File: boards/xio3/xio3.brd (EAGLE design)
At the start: 170 x 170 mm, 148 parts

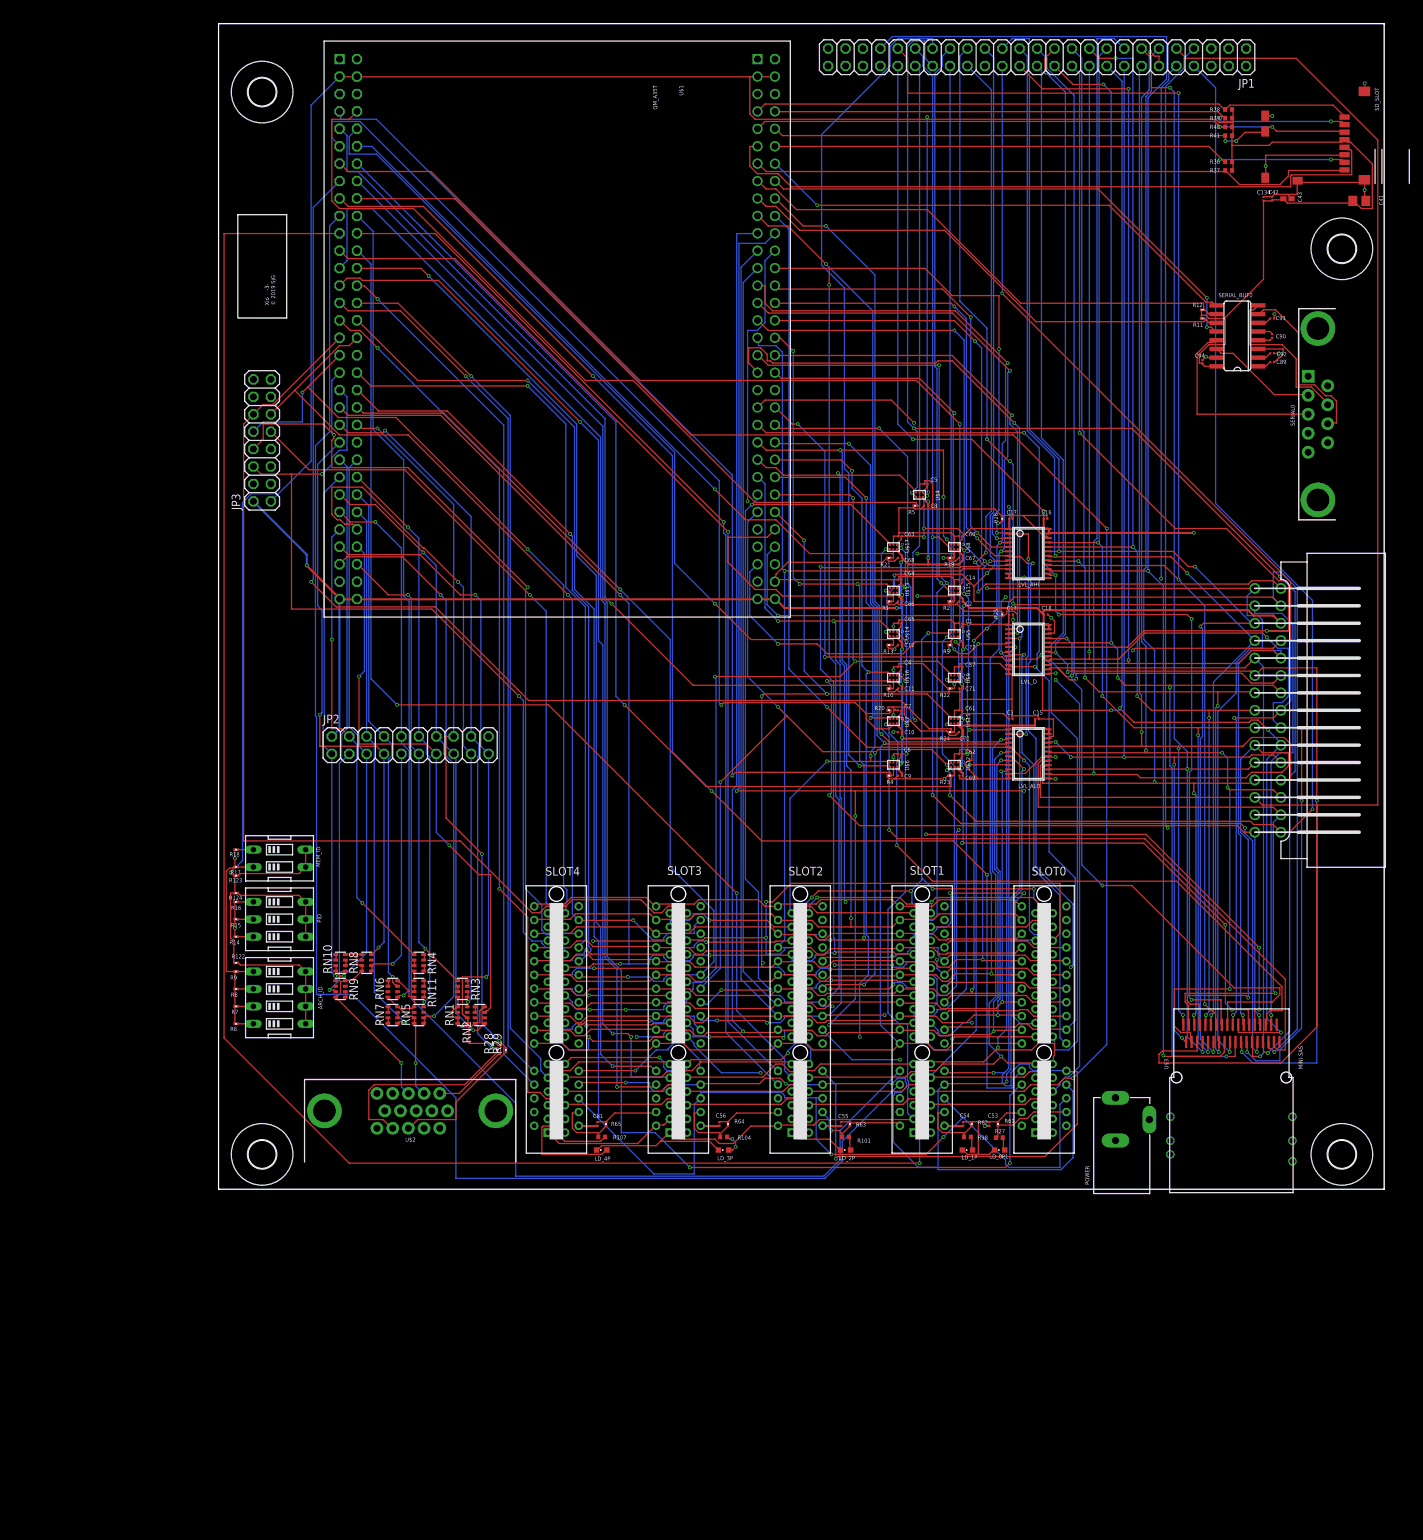
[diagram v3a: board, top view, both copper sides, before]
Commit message: - Add a +5v plane to cover where useful - Have a better placement of the HBUS extension - Gives at least 10cm of space for cards
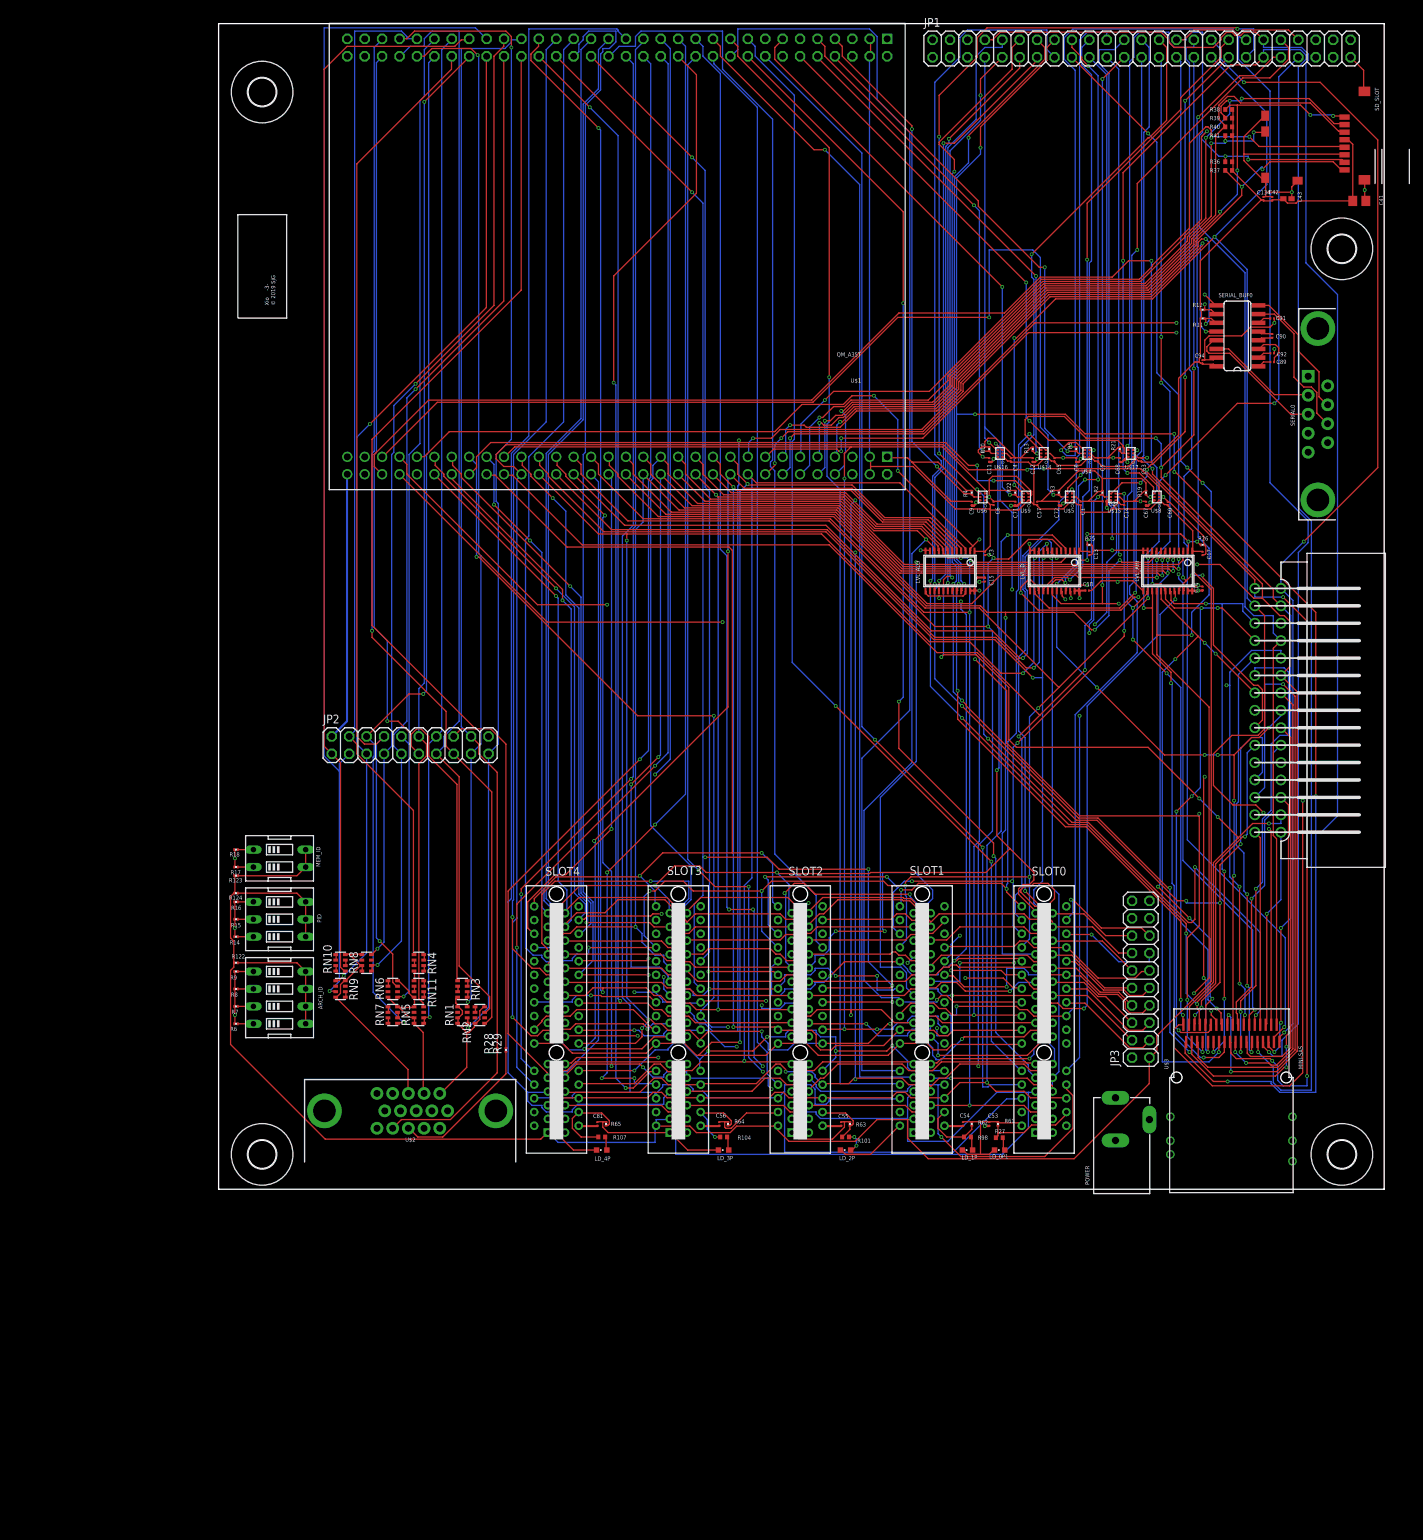
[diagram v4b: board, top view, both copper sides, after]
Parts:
- removed C10, C61, C62, C64, C66, C69, C7, C70: 0.1uF, rcl:C0201
- removed R1, R20, R23, R24: 10K, rcl:R0201
- removed U$11, U$12, U$13, U$7: 74LVC1T45GWSOT866, sjg-logic:SOT886
- JP3: device pinhead:2X08 -> pinhead:2X10
- moved JP3 150.3 mm to (134.5, 30.6)
- moved R4 43.0 mm to (109.9, 101.6), turned to 90 degrees
- moved U$6 41.2 mm to (111.4, 101.0), turned to 180 degrees
- moved C9 41.0 mm to (109.9, 100.0), turned to 90 degrees
- moved C6 39.0 mm to (113.0, 100.0), turned to 90 degrees
- moved R10 37.9 mm to (112.4, 108.0), turned to 90 degrees
- moved R21 37.2 mm to (131.4, 108.0), turned to 90 degrees
- moved U$17 37.2 mm to (133.0, 107.3), turned to 180 degrees
- moved C63 37.0 mm to (134.6, 106.4), turned to 90 degrees
- moved U$16 36.2 mm to (114.0, 107.3), turned to 180 degrees
- moved C11 35.8 mm to (112.4, 106.4), turned to 90 degrees
- moved R13 35.4 mm to (118.7, 108.0), turned to 90 degrees
- moved C68 35.1 mm to (131.4, 106.4), turned to 90 degrees
- moved U$14 34.3 mm to (120.3, 107.3), turned to 180 degrees
- moved C4 34.2 mm to (115.6, 106.4), turned to 90 degrees
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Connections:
- removed net !HI_REF!: JP1.40, U$3.PB16, U$7.4
- removed net !LO_S4!: SLOT0.B20, SLOT1.B20, SLOT2.B20, SLOT3.B20, SLOT4.B20, U$1.U7_53, U$12.3
- removed net !LO_S5!: SLOT0.B21, SLOT1.B21, SLOT2.B21, SLOT3.B21, SLOT4.B21, U$1.U7_54, U$11.3
- new net HBUS10: JP3.13, SLOT0.B28, SLOT1.B28, SLOT2.B28, SLOT3.B28, SLOT4.B28, U$1.U7_51
- new net HBUS11: JP3.14, SLOT0.B29, SLOT1.B29, SLOT2.B29, SLOT3.B29, SLOT4.B29, U$1.U7_52
- new net HBUS12: JP3.15, SLOT0.B30, SLOT1.B30, SLOT2.B30, SLOT3.B30, SLOT4.B30, U$1.U7_53
- new net HBUS13: JP3.16, SLOT0.B31, SLOT1.B31, SLOT2.B31, SLOT3.B31, SLOT4.B31, U$1.U7_54
- net !HI_CCTL!: no longer U$13.4
- net !HI_S4!: now also JP1.40, U$3.PB16; no longer U$12.4
- net !HI_S5!: now also JP1.44, U$3.PB18; no longer U$11.4
- net !LO_CCTL!: no longer U$1.U7_34, U$13.3
- net !LO_EXTSEL!: now also U$1.U7_43; no longer U$1.U7_44
- net !LO_HALT!: now also SLOT0.B13, SLOT1.B13, SLOT2.B13, SLOT3.B13, SLOT4.B13, U$1.U7_44; no longer SLOT0.A30, SLOT1.A30, SLOT2.A30, SLOT3.A30, SLOT4.A30, U$1.U7_45
- net !LO_IRQ!: now also SLOT0.B14, SLOT1.B14, SLOT2.B14, SLOT3.B14, SLOT4.B14, U$1.U7_45; no longer SLOT0.A31, SLOT1.A31, SLOT2.A31, SLOT3.A31, SLOT4.A31, U$1.U7_46
- net !LO_MPD!: now also SLOT0.A30, SLOT1.A30, SLOT2.A30, SLOT3.A30, SLOT4.A30, U$1.U7_46; no longer SLOT0.A32, SLOT1.A32, SLOT2.A32, SLOT3.A32, SLOT4.A32, U$1.U7_47
- net !LO_REF!: now also SLOT0.B15, SLOT1.B15, SLOT2.B15, SLOT3.B15, SLOT4.B15; no longer SLOT0.B17, SLOT1.B17, SLOT2.B17, SLOT3.B17, SLOT4.B17, U$1.U7_50, U$7.3
- net !LO_RST!: now also SLOT0.B16, SLOT1.B16, SLOT2.B16, SLOT3.B16, SLOT4.B16, U$1.U7_49; no longer SLOT0.B18, SLOT1.B18, SLOT2.B18, SLOT3.B18, SLOT4.B18, U$1.U7_51
- net +3V3: no longer C61.1, C62.1, C64.1, C7.1, U$11.1, U$12.1, U$13.1, U$7.1
- net +5V: no longer C10.1, C66.1, C69.1, C70.1, U$11.6, U$12.6, U$13.6, U$7.6
- net DIR_CCTL: no longer R1.1, U$13.5
- net DIR_REF: no longer R20.1, U$7.5
- net DIR_S4: no longer R23.1, U$12.5
- net DIR_S5: no longer R24.1, U$11.5
- net GND: now also JP3.17, JP3.18, JP3.19, JP3.20, SLOT0.B32, SLOT1.B32, SLOT2.B32, SLOT3.B32, SLOT4.B32; no longer C10.2, C61.2, C62.2, C64.2, C66.2, C69.2, C7.2, C70.2, JP1.44, JP3.13, JP3.14, JP3.15, JP3.16, R1.2, R20.2, R23.2, R24.2, SLOT0.A6, SLOT0.A7, SLOT1.A6, SLOT1.A7, SLOT2.A6, SLOT2.A7, SLOT3.A6, SLOT3.A7, SLOT4.A6, U$11.2, U$12.2, U$13.2, U$7.2
- net HBUS0: now also SLOT0.B18, SLOT1.B18, SLOT2.B18, SLOT3.B18, SLOT4.B18; no longer SLOT0.B22, SLOT1.B22, SLOT2.B22, SLOT3.B22, SLOT4.B22
- net HBUS1: now also SLOT0.B19, SLOT1.B19, SLOT2.B19, SLOT3.B19, SLOT4.B19; no longer SLOT0.B23, SLOT1.B23, SLOT2.B23, SLOT3.B23, SLOT4.B23
- net HBUS2: now also SLOT0.B20, SLOT1.B20, SLOT2.B20, SLOT3.B20, SLOT4.B20; no longer SLOT0.B24, SLOT1.B24, SLOT2.B24, SLOT3.B24, SLOT4.B24
- net HBUS3: now also SLOT0.B21, SLOT1.B21, SLOT2.B21, SLOT3.B21, SLOT4.B21; no longer SLOT0.B25, SLOT1.B25, SLOT2.B25, SLOT3.B25, SLOT4.B25
- net HBUS4: now also SLOT0.B22, SLOT1.B22, SLOT2.B22, SLOT3.B22, SLOT4.B22; no longer SLOT0.B26, SLOT1.B26, SLOT2.B26, SLOT3.B26, SLOT4.B26
- net HBUS5: now also SLOT0.B23, SLOT1.B23, SLOT2.B23, SLOT3.B23, SLOT4.B23; no longer SLOT0.B27, SLOT1.B27, SLOT2.B27, SLOT3.B27, SLOT4.B27
- net HBUS6: now also SLOT0.B24, SLOT1.B24, SLOT2.B24, SLOT3.B24, SLOT4.B24; no longer SLOT0.B28, SLOT1.B28, SLOT2.B28, SLOT3.B28, SLOT4.B28
- net HBUS7: now also SLOT0.B25, SLOT1.B25, SLOT2.B25, SLOT3.B25, SLOT4.B25; no longer SLOT0.B29, SLOT1.B29, SLOT2.B29, SLOT3.B29, SLOT4.B29
- net HBUS8: now also SLOT0.B26, SLOT1.B26, SLOT2.B26, SLOT3.B26, SLOT4.B26; no longer SLOT0.B30, SLOT1.B30, SLOT2.B30, SLOT3.B30, SLOT4.B30
- net HBUS9: now also SLOT0.B27, SLOT1.B27, SLOT2.B27, SLOT3.B27, SLOT4.B27; no longer SLOT0.B31, SLOT1.B31, SLOT2.B31, SLOT3.B31, SLOT4.B31
- net LO_CLK: now also U$1.U7_34; no longer U$1.U7_35
- net LO_D0: now also SLOT0.B5, SLOT1.B5, SLOT2.B5, SLOT3.B5, SLOT4.B5, U$1.U7_35; no longer SLOT0.B7, SLOT1.B7, SLOT2.B7, SLOT3.B7, SLOT4.B7, U$1.U7_36
- net LO_D1: now also SLOT0.B6, SLOT1.B6, SLOT2.B6, SLOT3.B6, SLOT4.B6, U$1.U7_36; no longer SLOT0.B8, SLOT1.B8, SLOT2.B8, SLOT3.B8, SLOT4.B8, U$1.U7_37
- net LO_D2: now also SLOT0.B7, SLOT1.B7, SLOT2.B7, SLOT3.B7, SLOT4.B7, U$1.U7_37; no longer SLOT0.B9, SLOT1.B9, SLOT2.B9, SLOT3.B9, SLOT4.B9, U$1.U7_38
- net LO_D3: now also SLOT0.B8, SLOT1.B8, SLOT2.B8, SLOT3.B8, SLOT4.B8, U$1.U7_38; no longer SLOT0.B10, SLOT1.B10, SLOT2.B10, SLOT3.B10, SLOT4.B10, U$1.U7_39
- net LO_D4: now also SLOT0.B9, SLOT1.B9, SLOT2.B9, SLOT3.B9, SLOT4.B9, U$1.U7_39; no longer SLOT0.B11, SLOT1.B11, SLOT2.B11, SLOT3.B11, SLOT4.B11, U$1.U7_40
- net LO_D5: now also SLOT0.B10, SLOT1.B10, SLOT2.B10, SLOT3.B10, SLOT4.B10, U$1.U7_40; no longer SLOT0.B12, SLOT1.B12, SLOT2.B12, SLOT3.B12, SLOT4.B12, U$1.U7_41
- net LO_D6: now also SLOT0.B11, SLOT1.B11, SLOT2.B11, SLOT3.B11, SLOT4.B11, U$1.U7_41; no longer SLOT0.B13, SLOT1.B13, SLOT2.B13, SLOT3.B13, SLOT4.B13, U$1.U7_42
- net LO_D7: now also SLOT0.B12, SLOT1.B12, SLOT2.B12, SLOT3.B12, SLOT4.B12, U$1.U7_42; no longer SLOT0.B14, SLOT1.B14, SLOT2.B14, SLOT3.B14, SLOT4.B14, U$1.U7_43
- net LO_R/!W!: now also SLOT0.B17, SLOT1.B17, SLOT2.B17, SLOT3.B17, SLOT4.B17, U$1.U7_50; no longer SLOT0.B19, SLOT1.B19, SLOT2.B19, SLOT3.B19, SLOT4.B19, U$1.U7_52
- net LO_RD4: now also SLOT0.A31, SLOT1.A31, SLOT2.A31, SLOT3.A31, SLOT4.A31, U$1.U7_47; no longer SLOT0.B15, SLOT1.B15, SLOT2.B15, SLOT3.B15, SLOT4.B15, U$1.U7_48
- net LO_RD5: now also SLOT0.A32, SLOT1.A32, SLOT2.A32, SLOT3.A32, SLOT4.A32, U$1.U7_48; no longer SLOT0.B16, SLOT1.B16, SLOT2.B16, SLOT3.B16, SLOT4.B16, U$1.U7_49
- net VALID_RD: now also SLOT0.A7, SLOT1.A7, SLOT2.A7, SLOT3.A7, SLOT4.A7; no longer SLOT0.B5, SLOT1.B5, SLOT2.B5, SLOT3.B5, SLOT4.B5
- net VALID_WR: now also SLOT0.A6, SLOT1.A6, SLOT2.A6, SLOT3.A6, SLOT4.A6; no longer SLOT0.B6, SLOT1.B6, SLOT2.B6, SLOT3.B6, SLOT4.B6
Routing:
- net +5V: track 337.0 -> 77.4 mm, vias 17 -> 13
- net !LO_S4!: track 230.6 -> 0.00 mm, vias 5 -> 0
- net !HI_REF!: track 193.0 -> 0.00 mm, vias 3 -> 0
- net HBUS11: track 0.00 -> 185.3 mm, vias 0 -> 1
- net !LO_S5!: track 176.6 -> 0.00 mm, vias 6 -> 0
- net HBUS12: track 0.00 -> 170.6 mm, vias 0 -> 3
- net HBUS10: track 0.00 -> 168.4 mm, vias 0 -> 2
- net DIR_S5: track 164.6 -> 0.00 mm, vias 1 -> 0
- net HBUS13: track 0.00 -> 164.5 mm, vias 0 -> 1
- net +3V3: track 687.3 -> 532.1 mm, vias 18 -> 0
- net DIR_S4: track 151.0 -> 0.00 mm, vias 1 -> 0
- net DIR_REF: track 146.8 -> 0.00 mm, vias 1 -> 0
- net DIR_HALT: track 28.4 -> 165.0 mm, vias 1 -> 2
- net !LO_CCTL!: track 192.7 -> 74.3 mm, vias 9 -> 0
- net VALID_RD: track 205.4 -> 316.5 mm, vias 2 -> 0
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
